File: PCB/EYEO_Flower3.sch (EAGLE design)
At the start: 70 parts, among them U1 ATSAMD21E17D-MUT, U10 AO3400ACON, U11 AO3400ACON, U12 TPS63070RNMR, U2 OPA2344UA, U3 XC6206P332MR-G, U4 AO3400ACON, U5 AO3400ACON, U6 AO3400ACON, U7 AO3400ACON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

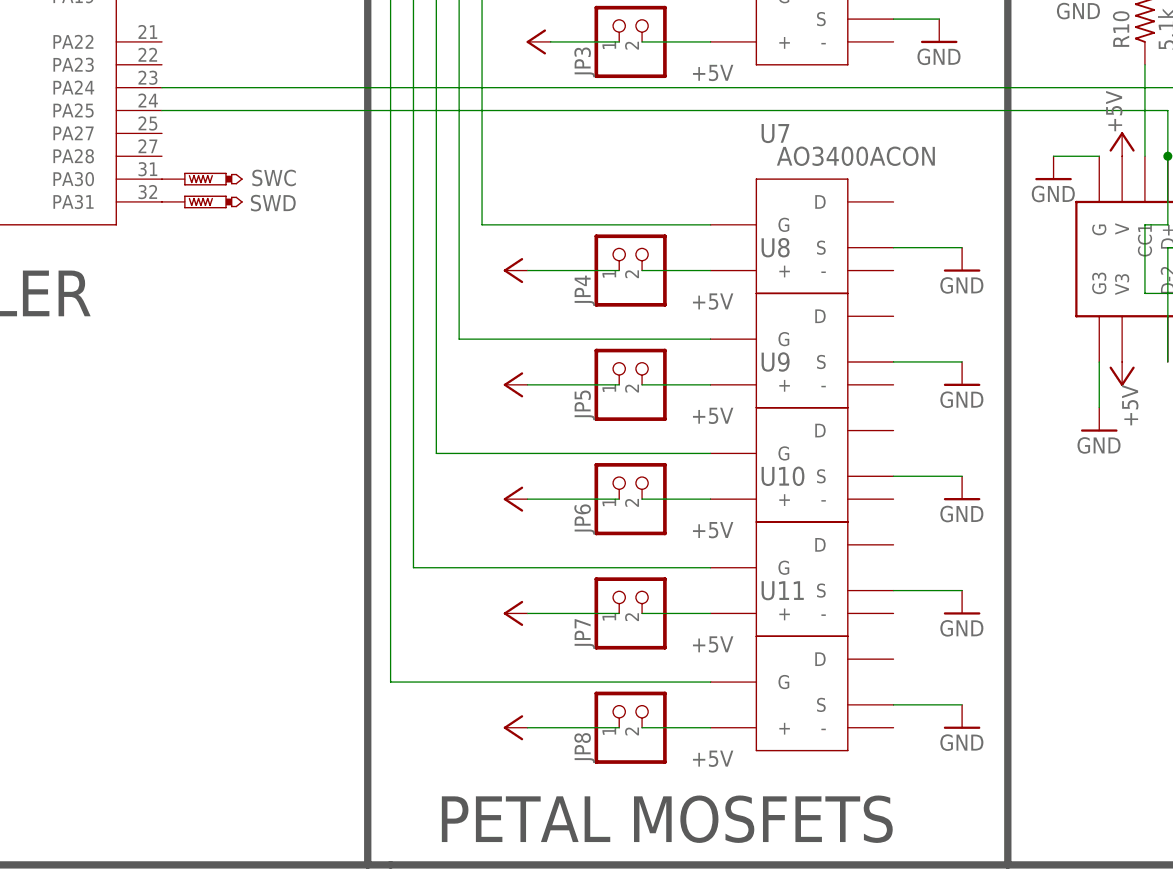
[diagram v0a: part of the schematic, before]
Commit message: Labeling nets for programmer
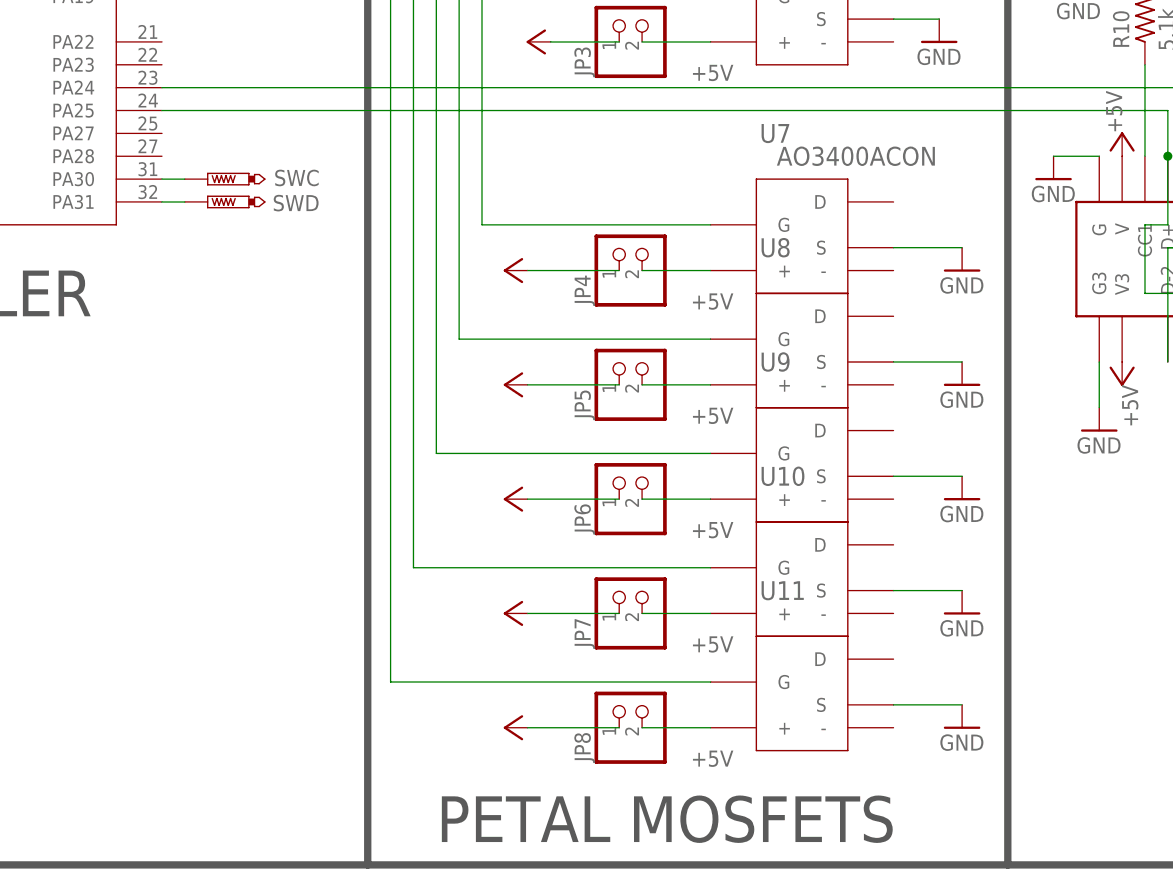
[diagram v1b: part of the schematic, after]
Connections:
- net N$10 renamed SWD
- net N$9 renamed SWC
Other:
- moved on the sheet: SWC, SWD
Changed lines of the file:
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@@
 <part name="U$2" library="Microphone" deviceset="B4013AM423" device="">
 <attribute name="LCSC_PART" value="C233794"/>
-<attribute name="NUM" value="B4013AM423-008
-"/>
+<attribute name="NUM" value="B4013AM423-008 "/>
 </part>
 <part name="GND20" library="supply1" library_urn="urn:adsk.eagle:library:371" deviceset="GND" device=""/>
@@
 <wire x1="142.24" y1="119.38" x2="142.24" y2="106.68" width="0.8128" layer="97"/>
 <wire x1="142.24" y1="106.68" x2="142.24" y2="-20.32" width="0.8128" layer="97"/>
-<wire x1="142.24" y1="-20.32" x2="73.66" y2="-20.32" width="0.8128" layer="97"/>
-<wire x1="73.66" y1="-20.32" x2="71.12" y2="-20.32" width="0.8128" layer="97"/>
+<wire x1="142.24" y1="-20.32" x2="71.12" y2="-20.32" width="0.8128" layer="97"/>
 <wire x1="71.12" y1="-20.32" x2="71.12" y2="83.82" width="0.8128" layer="97"/>
 <wire x1="71.12" y1="83.82" x2="86.36" y2="99.06" width="0.8128" layer="97"/>
@@
 <attribute name="LCSC_PART" x="144.78" y="142.24" size="1.778" layer="96" display="off"/>
 </instance>
-<instance part="SWC" gate="G$1" x="50.8" y="55.88" smashed="yes" rot="R90">
-<attribute name="NAME" x="63.246" y="56.896" size="1.778" layer="95" rot="R180"/>
-<attribute name="TP_SIGNAL_NAME" x="53.34" y="57.15" size="1.778" layer="97" rot="R90"/>
-</instance>
-<instance part="SWD" gate="G$1" x="50.8" y="53.34" smashed="yes" rot="R90">
-<attribute name="NAME" x="63.246" y="54.102" size="1.778" layer="95" rot="R180"/>
-<attribute name="TP_SIGNAL_NAME" x="53.34" y="54.61" size="1.778" layer="97" rot="R90"/>
+<instance part="SWC" gate="G$1" x="53.34" y="55.88" smashed="yes" rot="R90">
+<attribute name="NAME" x="65.786" y="56.896" size="1.778" layer="95" rot="R180"/>
+<attribute name="TP_SIGNAL_NAME" x="55.88" y="57.15" size="1.778" layer="97" rot="R90"/>
+</instance>
+<instance part="SWD" gate="G$1" x="53.34" y="53.34" smashed="yes" rot="R90">
+<attribute name="NAME" x="65.786" y="54.102" size="1.778" layer="95" rot="R180"/>
+<attribute name="TP_SIGNAL_NAME" x="55.88" y="54.61" size="1.778" layer="97" rot="R90"/>
 </instance>
 <instance part="GND14" gate="1" x="86.36" y="180.34" smashed="yes">
@@
 </segment>
 </net>
-<net name="N$9" class="0">
+<net name="SWC" class="0">
 <segment>
 <pinref part="U1" gate="A" pin="PA30"/>
 <pinref part="SWC" gate="G$1" pin="TP"/>
-</segment>
-</net>
-<net name="N$10" class="0">
+<wire x1="50.8" y1="55.88" x2="48.26" y2="55.88" width="0.1524" layer="91"/>
+</segment>
+</net>
+<net name="SWD" class="0">
 <segment>
 <pinref part="U1" gate="A" pin="PA31"/>
 <pinref part="SWD" gate="G$1" pin="TP"/>
-</segment>
-</net>
+<wire x1="50.8" y1="53.34" x2="48.26" y2="53.34" width="0.1524" layer="91"/>
+</segment>
+</net>
